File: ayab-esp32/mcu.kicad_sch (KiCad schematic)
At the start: 19 parts, among them Q301 AO3400A, SW301 RESET, SW302 BOOTSEL, U301 ESP32-S3-MINI-1

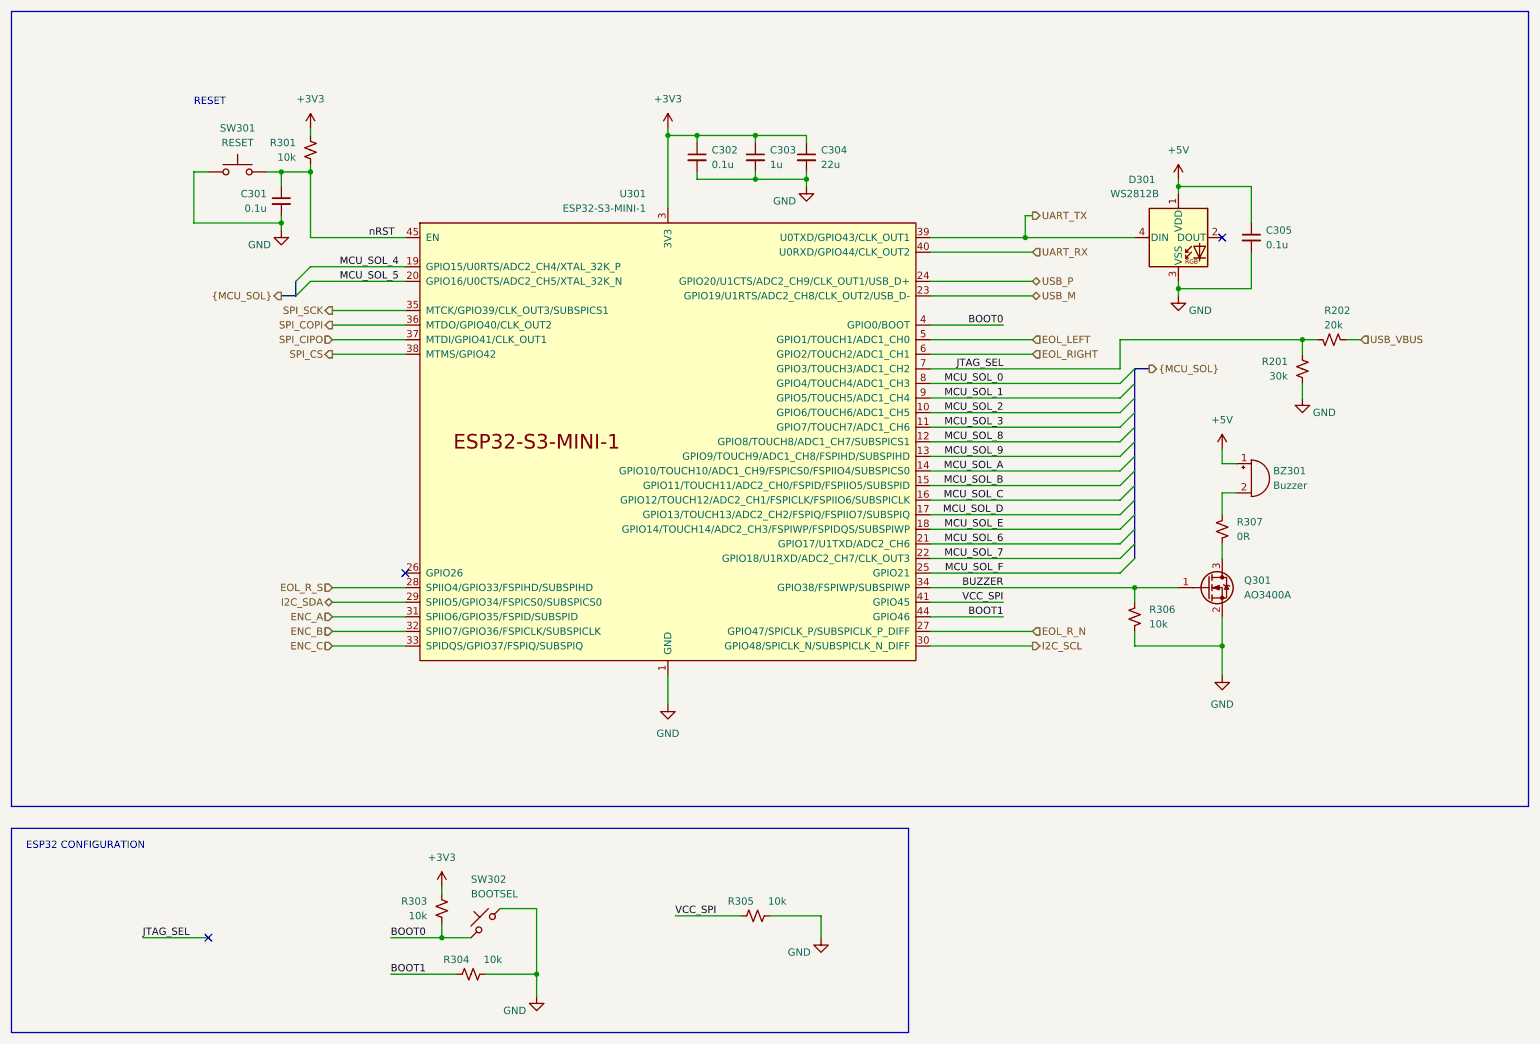
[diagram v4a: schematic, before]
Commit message: add ideal diode, remove extra uln2003a, add comparator for analog EOL sensors
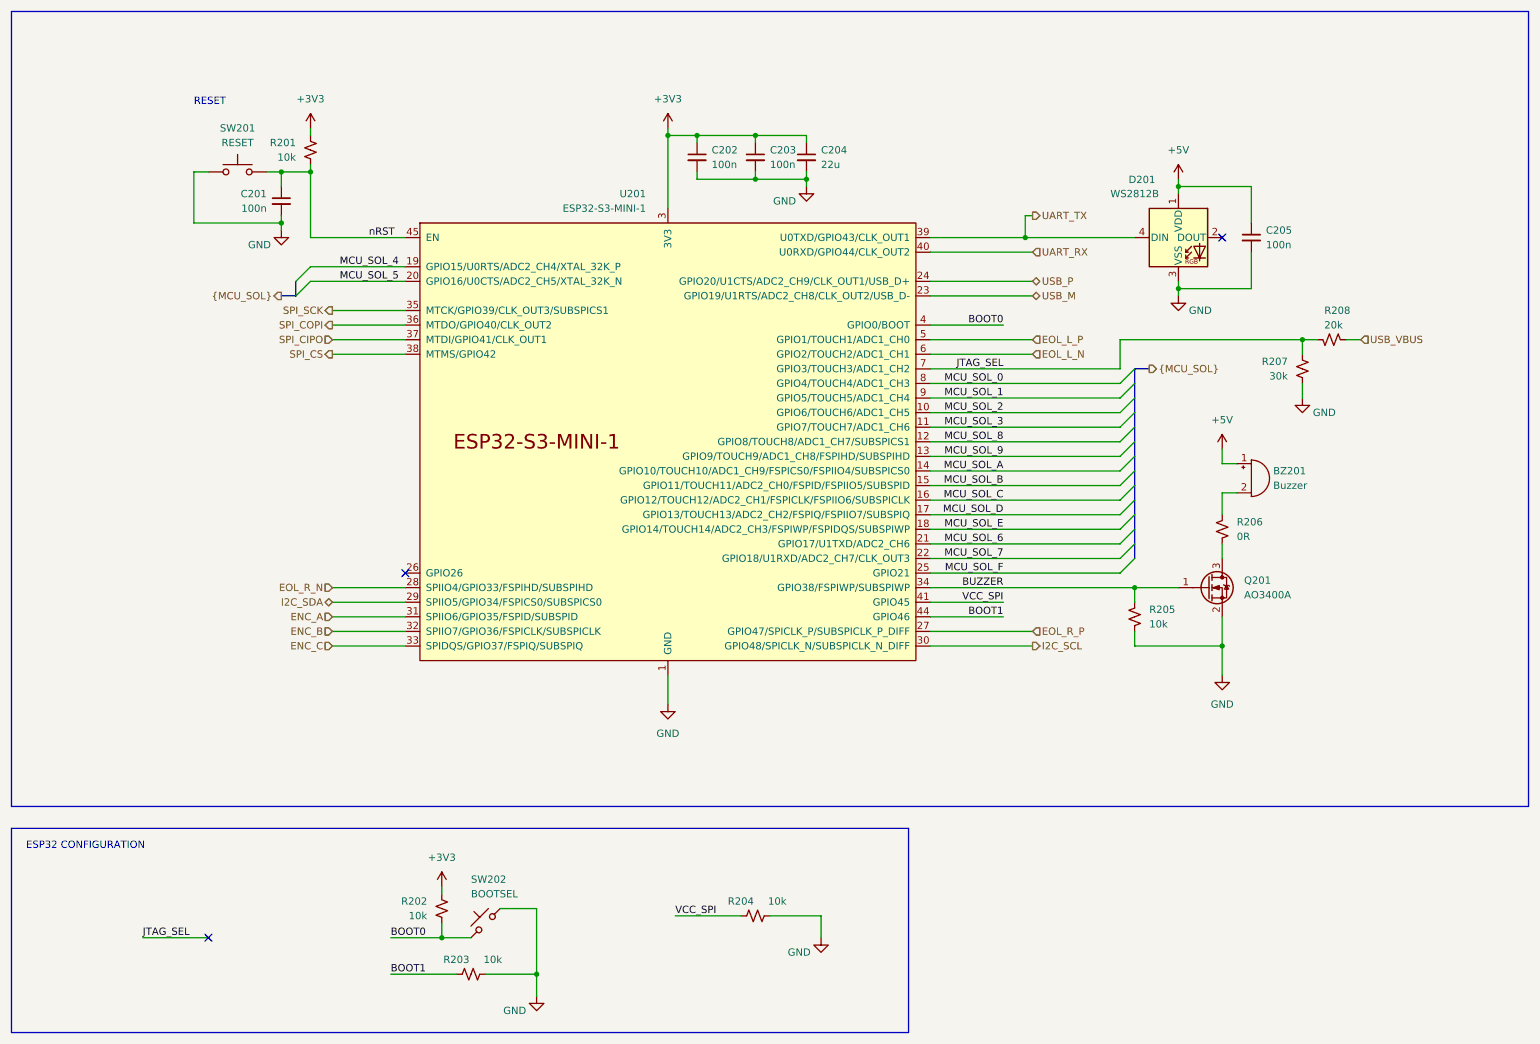
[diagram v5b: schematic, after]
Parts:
- C201: renamed from C301; value 0.1u -> 100n
- C202: renamed from C302; value 0.1u -> 100n
- C203: renamed from C303; value 1u -> 100n
- C205: renamed from C305; value 0.1u -> 100n
- renumbered BZ301 to BZ201, C304 to C204, D301 to D201, Q301 to Q201, R301 to R201, R303 to R202, R304 to R203, R305 to R204, R306 to R205, R307 to R206, R201 to R207, R202 to R208, SW301 to SW201, SW302 to SW202, U301 to U201
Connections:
- net EOL_R_S is gone; now on net EOL_R_N: U201.28 (SPIIO4/GPIO33/FSPIHD/SUBSPIHD)
- net EOL_R_N: no longer U201.27 (GPIO47/SPICLK_P/SUBSPICLK_P_DIFF)
- net EOL_LEFT renamed EOL_L_P
- net EOL_RIGHT renamed EOL_L_N
- new net EOL_R_P: U201.27 (GPIO47/SPICLK_P/SUBSPICLK_P_DIFF)

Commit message: fix comparator
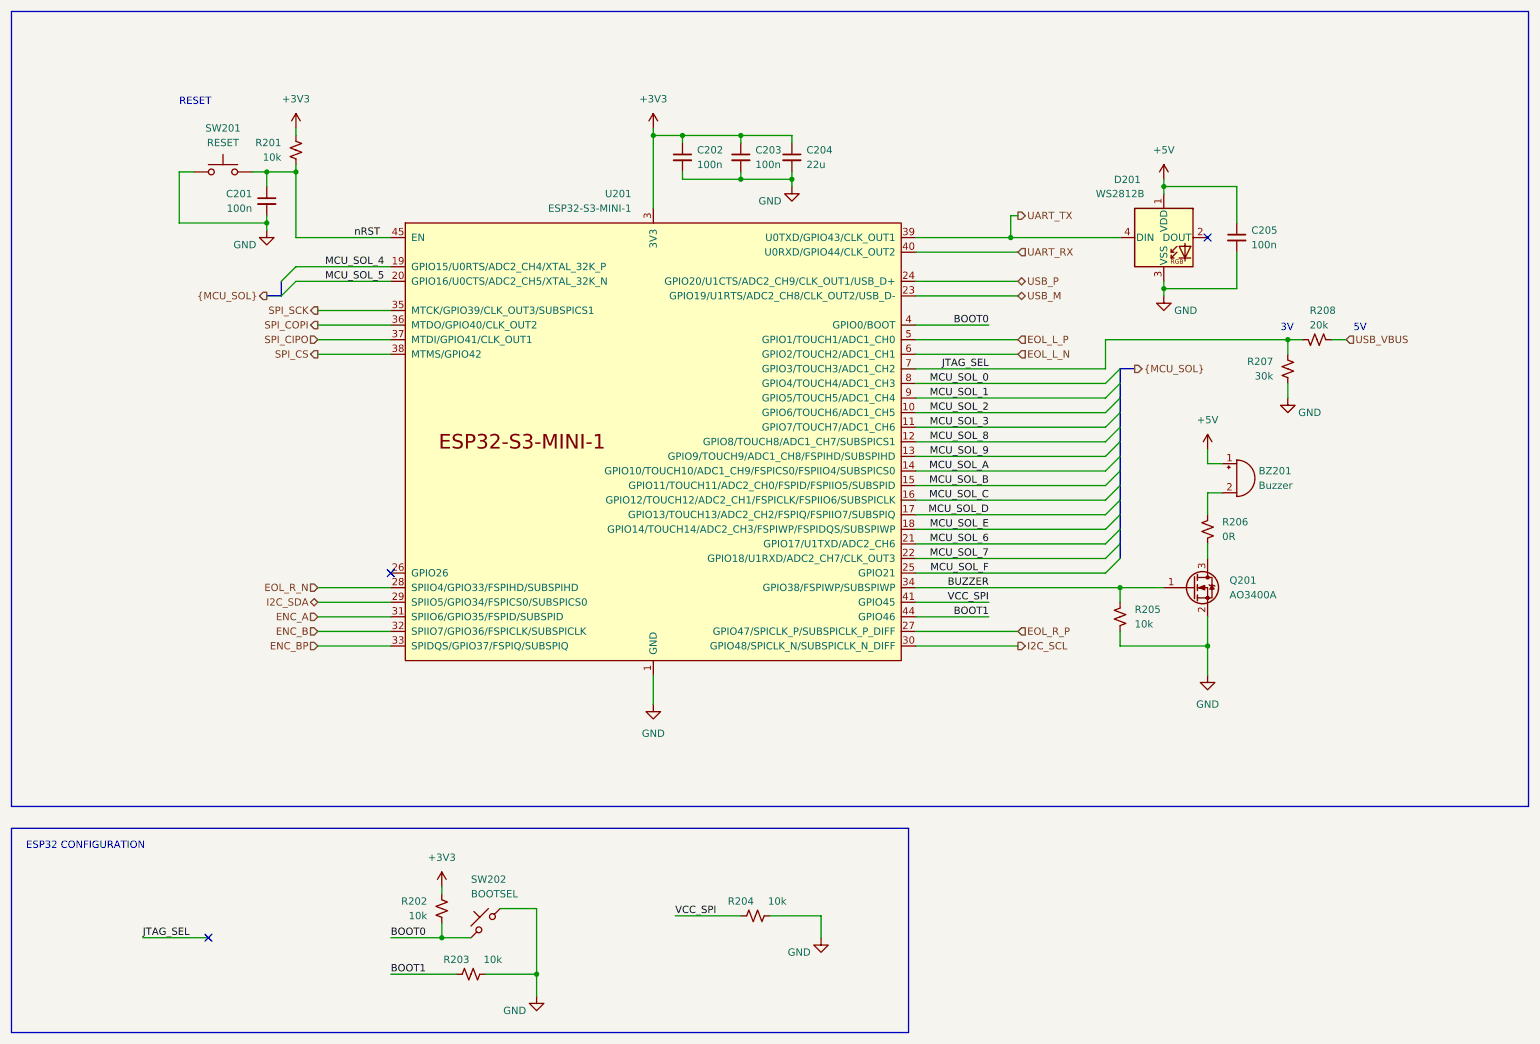
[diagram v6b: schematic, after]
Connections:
- net ENC_C renamed ENC_BP
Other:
- note added: "3V"
- note added: "5V"
- moved on the sheet: BZ201, C201, C202, C203, C204, C205, D201, Q201, R201, R205, R206, R207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

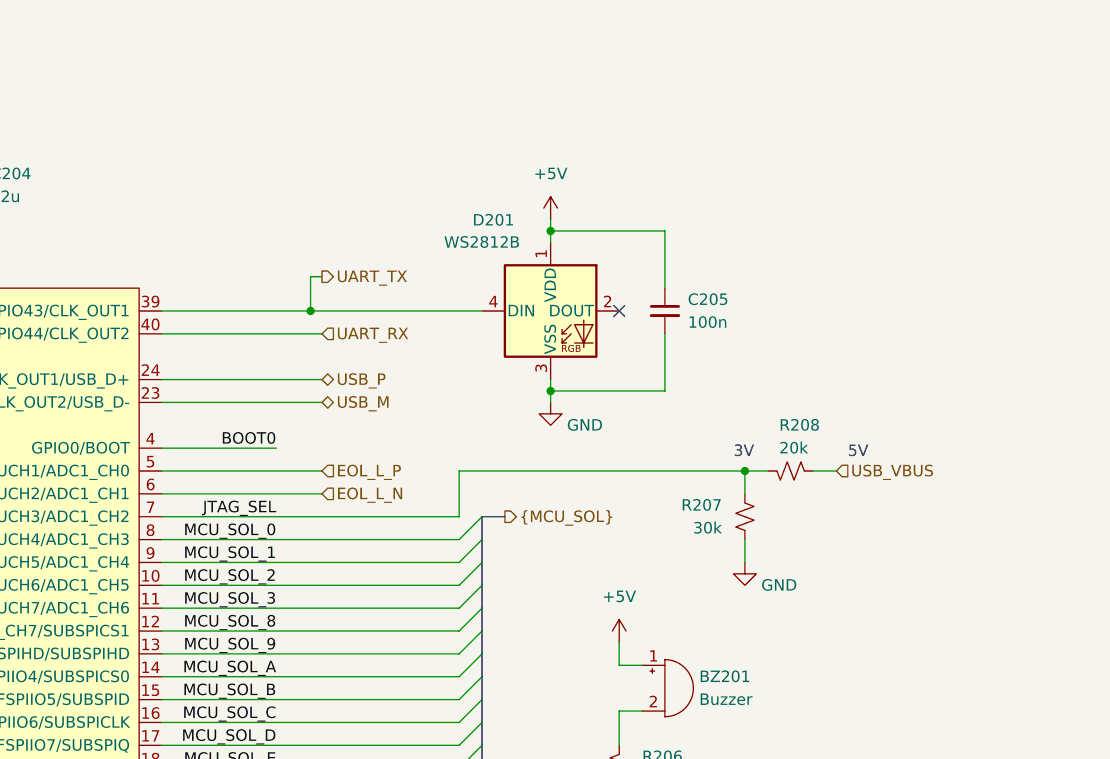
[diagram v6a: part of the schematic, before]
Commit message: fix folder structure and update gitignore
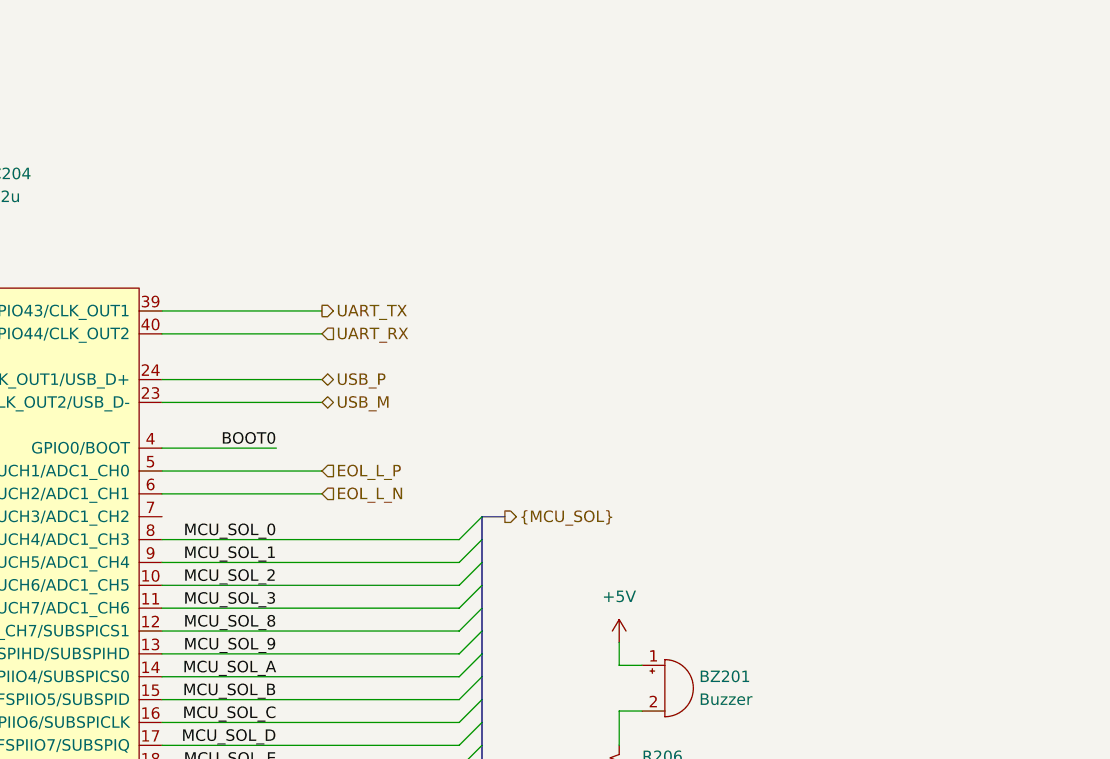
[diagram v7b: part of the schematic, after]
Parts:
- removed C205: 100n, symbol Device:C_Small
- removed D201: WS2812B, LED_SMD:LED_WS2812B_PLCC4_5.0x5.0mm_P3.2mm, symbol LED:WS2812B
- removed R207: 30k, symbol Device:R_Small_US
- removed R208: 20k, symbol Device:R_Small_US
- BZ201: symbol Device:Buzzer -> ayab-esp32:Buzzer
- C201, C202, C203, C204: symbol Device:C_Small -> ayab-esp32:C_Small
- Q201: symbol Transistor_FET:AO3400A -> ayab-esp32:AO3400A
- R201, R202, R203, R204, R205, R206: symbol Device:R_Small_US -> ayab-esp32:R_Small_US
- SW201: symbol Switch:SW_Push -> ayab-esp32:SW_Push
- SW202: symbol Switch:SW_Push_45deg -> ayab-esp32:SW_Push_45deg
- U201: symbol Espressif:ESP32-S3-MINI-1 -> ayab-esp32:ESP32-S3-MINI-1
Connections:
- net JTAG_SEL: no longer U201.7 (GPIO3/TOUCH3/ADC1_CH2)
- no-connect marks 3 -> 2
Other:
- note removed: "3V"
- note removed: "5V"

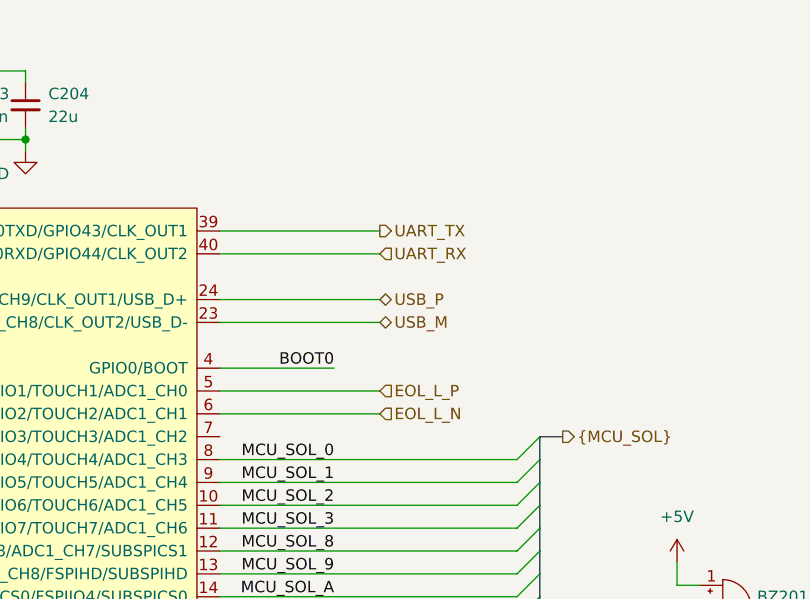
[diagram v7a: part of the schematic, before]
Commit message: comparator biasing and cleanup
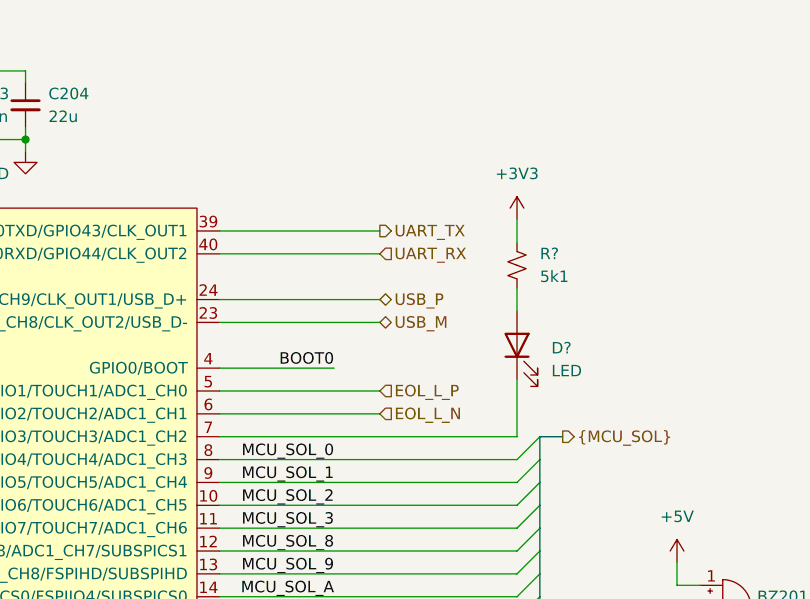
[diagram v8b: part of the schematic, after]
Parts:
- added D?: LED, symbol ayab-esp32:LED
- added R?: 5k1, symbol ayab-esp32:R_Small_US
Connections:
- net +3V3: now also R?.1
- net at U201.7 (GPIO3/TOUCH3/ADC1_CH2): now also D?.1 (K)
- new net: D?.2 (A), R?.2
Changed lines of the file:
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@@
     (stroke (width 0) (type default))
   )
+  (wire (pts (xy 207.01 62.23) (xy 207.01 64.77))
+    (stroke (width 0) (type default))
+  )
   (bus (pts (xy 209.55 96.52) (xy 209.55 99.06))
     (stroke (width 0) (type default))
@@
     (stroke (width 0) (type default))
   )
+  (wire (pts (xy 207.01 78.74) (xy 173.99 78.74))
+    (stroke (width 0) (type default))
+  )
   (wire (pts (xy 60.96 52.07) (xy 60.96 53.34))
     (stroke (width 0) (type default))
@@
     (stroke (width 0) (type default))
   )
+  (wire (pts (xy 207.01 54.61) (xy 207.01 57.15))
+    (stroke (width 0) (type default))
+  )
   (bus (pts (xy 209.55 91.44) (xy 209.55 93.98))
     (stroke (width 0) (type default))
@@
     (stroke (width 0) (type default))
   )
+  (wire (pts (xy 207.01 72.39) (xy 207.01 78.74))
+    (stroke (width 0) (type default))
+  )
   (wire (pts (xy 173.99 111.76) (xy 207.01 111.76))
     (stroke (width 0) (type default))
@@
     )
   )
+  (symbol (lib_id "ayab-esp32:R_Small_US") (at 207.01 59.69 0) (unit 1)
+    (in_bom yes) (on_board yes) (dnp no) (fields_autoplaced)
+    (property "Reference" "R?" (at 209.55 58.42 0)
+      (effects (font (size 1.27 1.27)) (justify left))
+    )
+    (property "Value" "5k1" (at 209.55 60.96 0)
+      (effects (font (size 1.27 1.27)) (justify left))
+    )
+    (property "Footprint" "" (at 207.01 59.69 0)
+      (effects (font (size 1.27 1.27)) hide)
+    )
+    (property "Datasheet" "~" (at 207.01 59.69 0)
+      (effects (font (size 1.27 1.27)) hide)
+    )
+    (pin "1")
+    (pin "2")
+    (instances
+      (project "ayab-esp32"
+        (path "/ad16b75f-afc8-4717-a7c6-8dd7b69a18e2/a7e0db0f-e473-44d4-a2fe-681f732aacb2"
+          (reference "R?") (unit 1)
+        )
+      )
+    )
+  )
+  (symbol (lib_id "ayab-esp32:LED") (at 207.01 68.58 90) (unit 1)
+    (in_bom yes) (on_board yes) (dnp no) (fields_autoplaced)
+    (property "Reference" "D?" (at 210.82 68.8975 90)
+      (effects (font (size 1.27 1.27)) (justify right))
+    )
+    (property "Value" "LED" (at 210.82 71.4375 90)
+      (effects (font (size 1.27 1.27)) (justify right))
+    )
+    (property "Footprint" "" (at 207.01 68.58 0)
+      (effects (font (size 1.27 1.27)) hide)
+    )
+    (property "Datasheet" "~" (at 207.01 68.58 0)
+      (effects (font (size 1.27 1.27)) hide)
+    )
+    (pin "1")
+    (pin "2")
+    (instances
+      (project "ayab-esp32"
+        (path "/ad16b75f-afc8-4717-a7c6-8dd7b69a18e2/a7e0db0f-e473-44d4-a2fe-681f732aacb2"
+          (reference "D?") (unit 1)
+        )
+      )
+    )
+  )
   (symbol (lib_id "power:+3V3") (at 66.04 36.83 0) (unit 1)
     (in_bom yes) (on_board yes) (dnp no) (fields_autoplaced)
@@
         )
       )
+    )
+  )
+  (symbol (lib_id "power:+3V3") (at 207.01 54.61 0) (unit 1)
+    (in_bom yes) (on_board yes) (dnp no) (fields_autoplaced)
+    (property "Reference" "#PWR0209" (at 207.01 58.42 0)
+      (effects (font (size 1.27 1.27)) hide)
+    )
+    (property "Value" "+3V3" (at 207.01 49.53 0)
+      (effects (font (size 1.27 1.27)))
+    )
+    (property "Footprint" "" (at 207.01 54.61 0)
+      (effects (font (size 1.27 1.27)) hide)
+    )
+    (property "Datasheet" "" (at 207.01 54.61 0)
+      (effects (font (size 1.27 1.27)) hide)
+    )
+    (pin "1")
+    (instances
+      (project "ayab-esp32"
+        (path "/ad16b75f-afc8-4717-a7c6-8dd7b69a18e2/a7e0db0f-e473-44d4-a2fe-681f732aacb2"
+          (reference "#PWR0209") (unit 1)
+        )
+      )
